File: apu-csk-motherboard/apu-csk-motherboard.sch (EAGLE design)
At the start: 17 parts

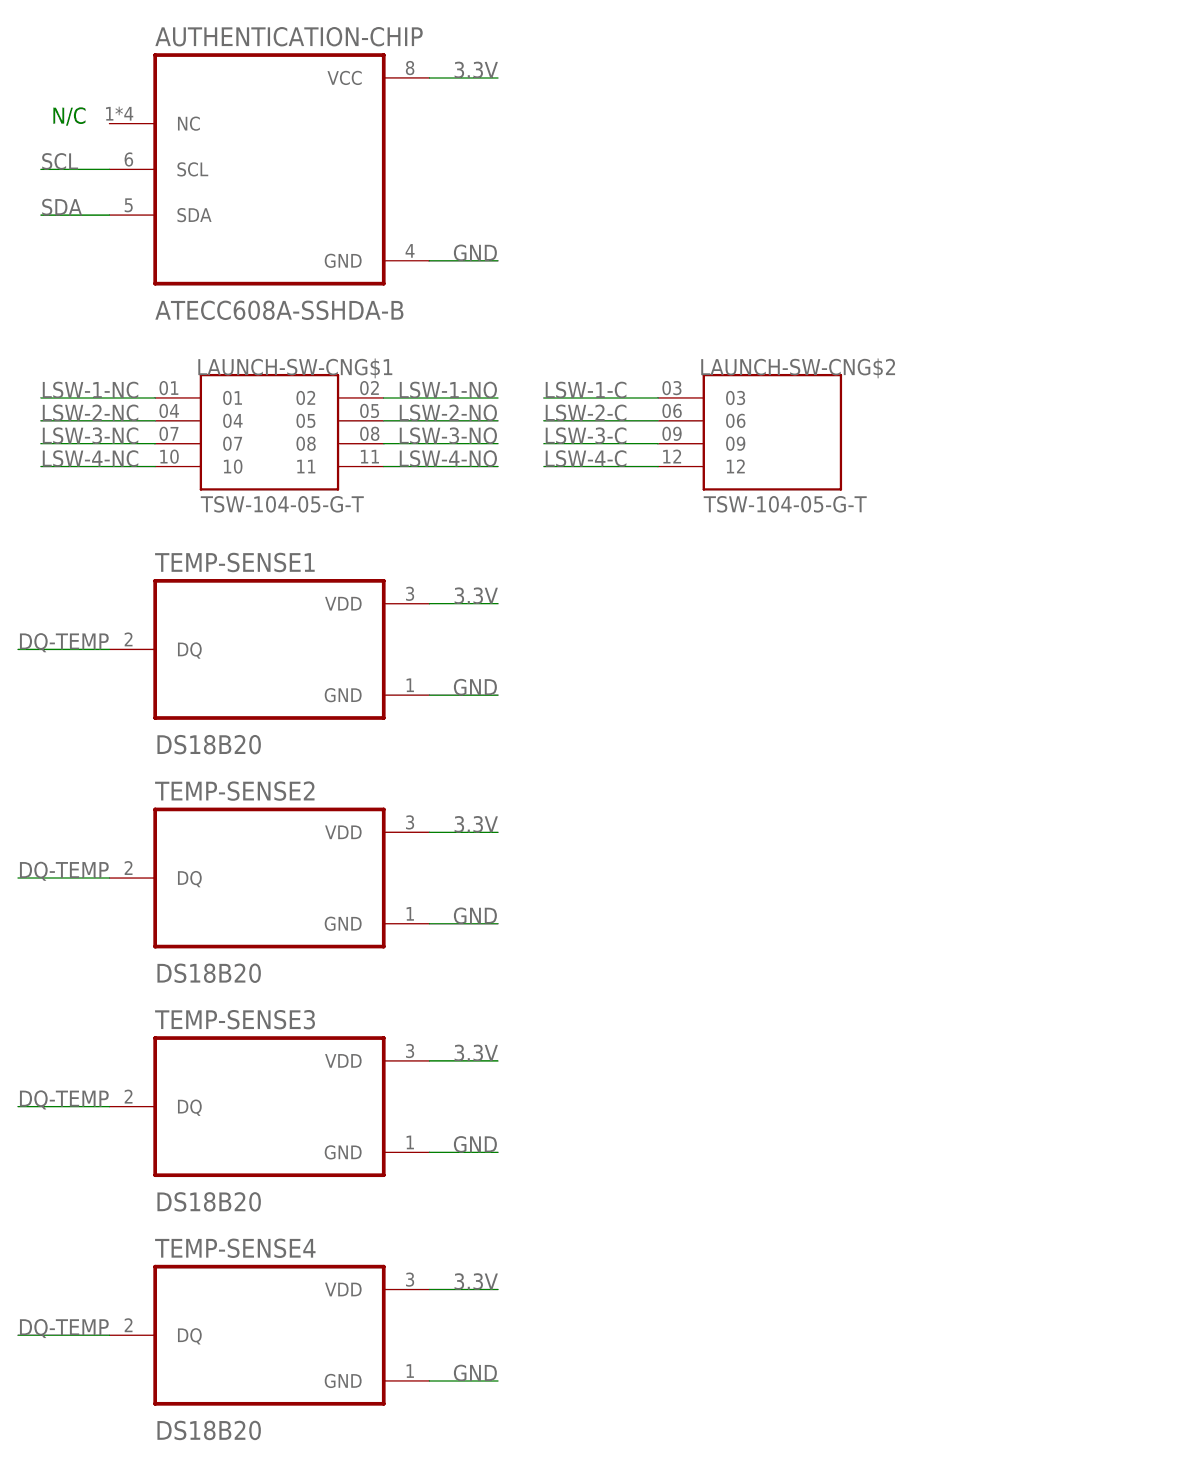
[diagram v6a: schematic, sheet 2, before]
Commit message: Added FRAM and RTC but need to finish connections
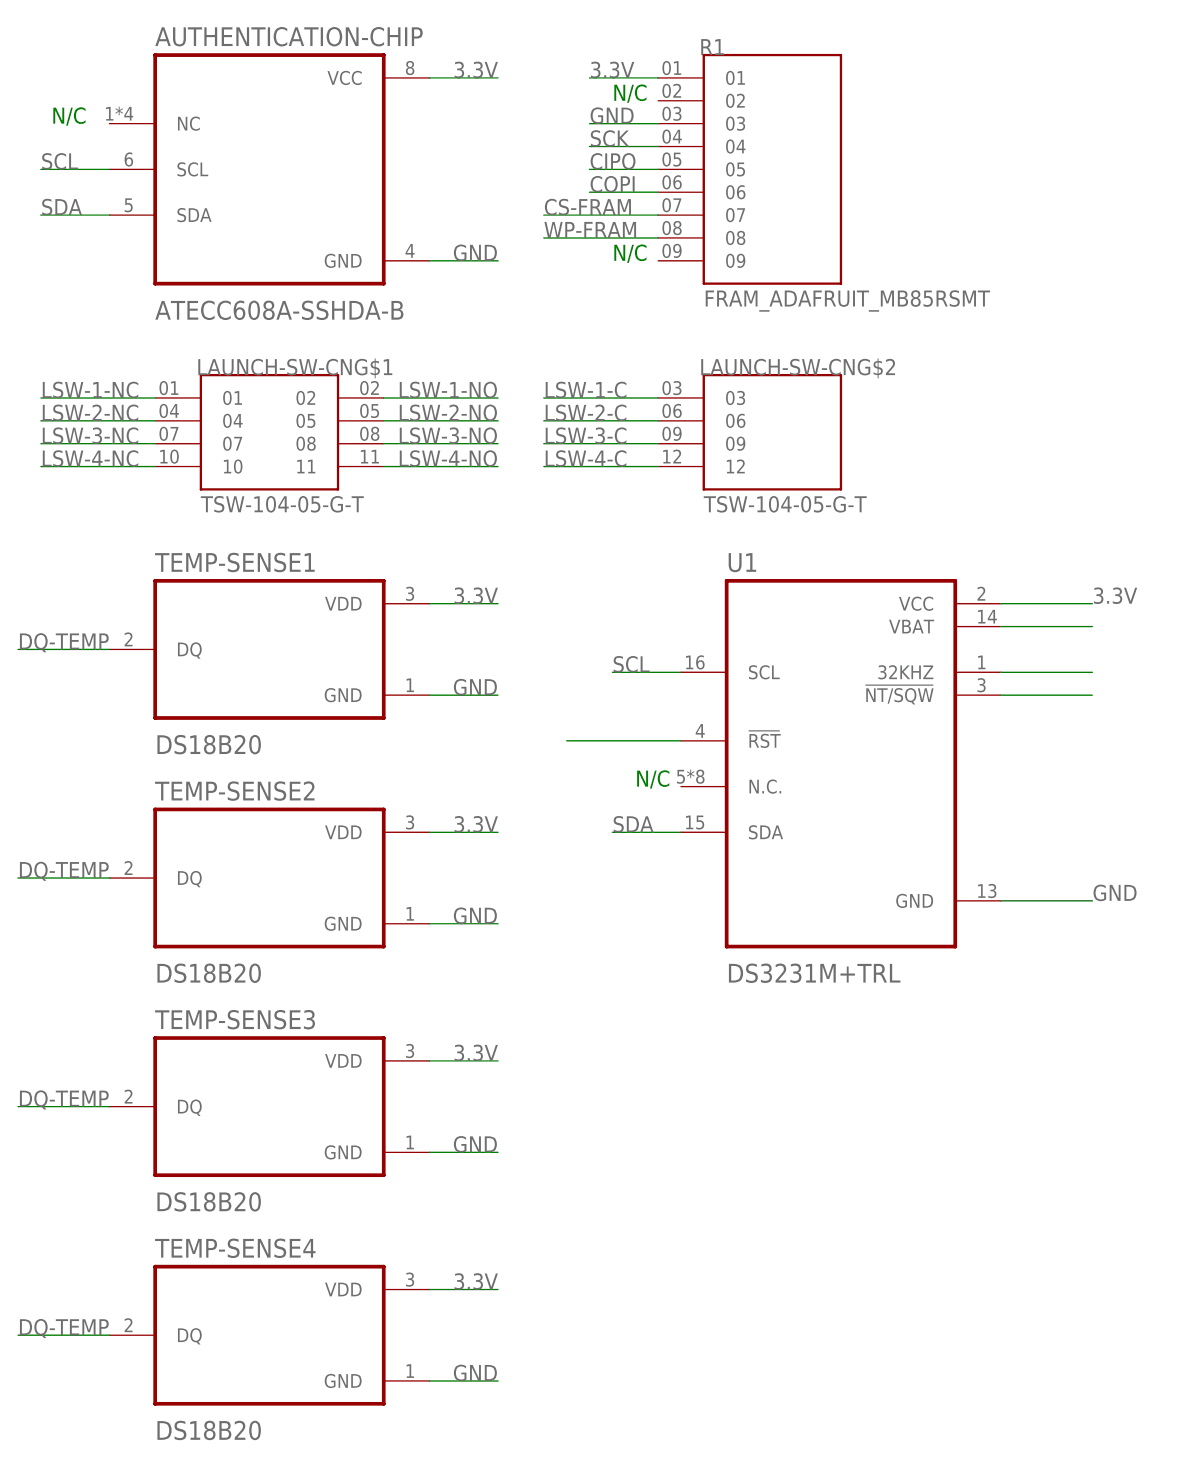
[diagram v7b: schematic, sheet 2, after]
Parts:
- added R1: FRAM_ADAFRUIT_MB85RSMT, apu-csk-motherboard:FRAM_ADAFRUIT_MB85RSMT
- added U1: DS3231M+TRL, DS3231M_TRL:DS3231M+TRL
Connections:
- new net CS-FRAM: FEATHER1-16.IO20@T10, R1.07
- new net N$11: U1.!NT/SQW
- new net N$6: U1.VBAT
- new net N$9: U1.!RST
- new net RTCLOCK: U1.32KHZ
- new net WP-FRAM: FEATHER1-12.IO0@B3, R1.08
- net 3.3V: now also R1.01, U1.VCC
- net CIPO: now also R1.05
- net COPI: now also R1.06
- net GND: now also R1.03, U1.GND
- net SCK: now also R1.04
- net SCL: now also U1.SCL
- net SDA: now also U1.SDA
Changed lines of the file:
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@@
 <layer number="59" name="tCarbon" color="7" fill="1" visible="no" active="no"/>
 <layer number="60" name="bCarbon" color="7" fill="1" visible="no" active="no"/>
+<layer number="61" name="stand" color="7" fill="1" visible="no" active="no"/>
 <layer number="88" name="SimResults" color="9" fill="1" visible="yes" active="yes"/>
 <layer number="89" name="SimProbes" color="9" fill="1" visible="yes" active="yes"/>
@@
 <layer number="112" name="tSilk" color="7" fill="1" visible="no" active="yes"/>
 <layer number="113" name="IDFDebug" color="4" fill="1" visible="no" active="yes"/>
+<layer number="114" name="tPlaceRed" color="7" fill="1" visible="yes" active="yes"/>
+<layer number="115" name="FRNTMAAT2" color="7" fill="1" visible="yes" active="yes"/>
 <layer number="116" name="Patch_BOT" color="9" fill="4" visible="no" active="yes"/>
+<layer number="117" name="BACKMAAT1" color="7" fill="1" visible="yes" active="yes"/>
 <layer number="118" name="Rect_Pads" color="7" fill="1" visible="no" active="yes"/>
+<layer number="119" name="KAP_TEKEN" color="7" fill="1" visible="yes" active="yes"/>
+<layer number="120" name="KAP_MAAT1" color="7" fill="1" visible="yes" active="yes"/>
 <layer number="121" name="_tsilk" color="7" fill="1" visible="no" active="yes"/>
 <layer number="122" name="_bsilk" color="7" fill="1" visible="no" active="yes"/>
@@
 <layer number="128" name="_bValues" color="7" fill="1" visible="no" active="yes"/>
 <layer number="129" name="Mask" color="7" fill="1" visible="no" active="yes"/>
+<layer number="130" name="SMDSTROOK" color="7" fill="1" visible="yes" active="yes"/>
 <layer number="131" name="tAdjust" color="7" fill="1" visible="no" active="yes"/>
 <layer number="132" name="bAdjust" color="7" fill="1" visible="no" active="yes"/>
+<layer number="133" name="bottom_silk" color="7" fill="1" visible="yes" active="yes"/>
+<layer number="134" name="silk_top" color="7" fill="1" visible="no" active="yes"/>
+<layer number="135" name="silk_bottom" color="7" fill="1" visible="no" active="yes"/>
+<layer number="136" name="silktop" color="7" fill="1" visible="no" active="yes"/>
+<layer number="137" name="silkbottom" color="7" fill="1" visible="no" active="yes"/>
+<layer number="138" name="EEE" color="7" fill="1" visible="no" active="yes"/>
+<layer number="139" name="_tKeepout" color="7" fill="1" visible="no" active="yes"/>
+<layer number="140" name="mbKeepout" color="7" fill="1" visible="no" active="yes"/>
+<layer number="141" name="ASSEMBLY_TOP" color="7" fill="1" visible="no" active="yes"/>
+<layer number="142" name="mbRestrict" color="7" fill="1" visible="no" active="yes"/>
+<layer number="143" name="PLACE_BOUND_TOP" color="7" fill="1" visible="no" active="yes"/>
 <layer number="144" name="Drill_legend" color="7" fill="1" visible="no" active="yes"/>
+<layer number="145" name="DrillLegend_01-16" color="7" fill="1" visible="no" active="yes"/>
+<layer number="146" name="DrillLegend_01-20" color="7" fill="1" visible="no" active="yes"/>
+<layer number="147" name="PIN_NUMBER" color="7" fill="1" visible="no" active="yes"/>
+<layer number="148" name="mDocument" color="7" fill="1" visible="no" active="yes"/>
+<layer number="149" name="DrillLegend_02-15" color="7" fill="1" visible="no" active="yes"/>
 <layer number="150" name="Notes" color="7" fill="1" visible="no" active="yes"/>
 <layer number="151" name="HeatSink" color="7" fill="1" visible="no" active="yes"/>
@@
 <layer number="154" name="FabDoc2" color="7" fill="1" visible="no" active="yes"/>
 <layer number="155" name="FabDoc3" color="7" fill="1" visible="no" active="yes"/>
+<layer number="166" name="AntennaArea" color="7" fill="1" visible="no" active="yes"/>
+<layer number="168" name="4mmHeightArea" color="7" fill="1" visible="no" active="yes"/>
+<layer number="191" name="mNets" color="7" fill="1" visible="no" active="yes"/>
+<layer number="192" name="mBusses" color="7" fill="1" visible="no" active="yes"/>
+<layer number="193" name="mPins" color="7" fill="1" visible="no" active="yes"/>
+<layer number="194" name="mSymbols" color="7" fill="1" visible="no" active="yes"/>
+<layer number="195" name="mNames" color="7" fill="1" visible="no" active="yes"/>
+<layer number="196" name="mValues" color="7" fill="1" visible="no" active="yes"/>
 <layer number="199" name="Contour" color="7" fill="1" visible="no" active="yes"/>
 <layer number="200" name="200bmp" color="1" fill="10" visible="no" active="yes"/>
@@
 <part name="TEMP-SENSE4" library="DS18B20" deviceset="DS18B20" device=""/>
 <part name="FRAME3" library="apu-csk-motherboard" deviceset="FRAME_LETTER_LANDSCAPE" device=""/>
+<part name="R1" library="apu-csk-motherboard" deviceset="FRAM_ADAFRUIT_MB85RSMT" device=""/>
+<part name="U1" library="DS3231M_TRL" deviceset="DS3231M+TRL" device=""/>
 </parts>
 <sheets>
@@
 </segment>
 </net>
+<net name="CS-FRAM" class="0">
+<segment>
+<pinref part="FEATHER1" gate="-16" pin="IO20@T10"/>
+<wire x1="154.94" y1="132.08" x2="167.64" y2="132.08" width="0.1524" layer="91"/>
+<label x="154.94" y="132.08" size="1.778" layer="95"/>
+</segment>
+</net>
+<net name="WP-FRAM" class="0">
+<segment>
+<pinref part="FEATHER1" gate="-12" pin="IO0@B3"/>
+<wire x1="154.94" y1="83.82" x2="167.64" y2="83.82" width="0.1524" layer="91"/>
+<label x="154.94" y="83.82" size="1.778" layer="95"/>
+</segment>
+</net>
 </nets>
 </sheet>
@@
 <plain>
 <text x="12.7" y="172.72" size="1.778" layer="91" rot="MR0">N/C</text>
+<text x="71.12" y="175.26" size="1.778" layer="91">N/C</text>
+<text x="71.12" y="157.48" size="1.778" layer="91">N/C</text>
+<text x="73.66" y="99.06" size="1.778" layer="91">N/C</text>
 </plain>
 <instances>
@@
 <attribute name="VALUE" x="20.32" y="26.48" size="2.0828" layer="96" ratio="10" rot="SR0"/>
 </instance>
+<instance part="R1" gate="G$1" x="88.9" y="167.64" smashed="yes">
+<attribute name="NAME" x="80.78" y="180.34" size="1.778" layer="95"/>
+<attribute name="VALUE" x="81.28" y="152.4" size="1.778" layer="96"/>
+</instance>
+<instance part="U1" gate="A" x="96.52" y="101.6" smashed="yes">
+<attribute name="NAME" x="83.82" y="122.92" size="2.0828" layer="95" ratio="10" rot="SR0"/>
+<attribute name="VALUE" x="83.82" y="77.28" size="2.0828" layer="96" ratio="10" rot="SR0"/>
+</instance>
 </instances>
 <busses>
@@
 <label x="58.42" y="157.48" size="1.778" layer="95" rot="MR0"/>
 </segment>
+<segment>
+<wire x1="68.58" y1="172.72" x2="76.2" y2="172.72" width="0.1524" layer="91"/>
+<label x="68.58" y="172.72" size="1.778" layer="95"/>
+<pinref part="R1" gate="G$1" pin="03"/>
+</segment>
+<segment>
+<pinref part="U1" gate="A" pin="GND"/>
+<wire x1="114.3" y1="86.36" x2="124.46" y2="86.36" width="0.1524" layer="91"/>
+<label x="124.46" y="86.36" size="1.778" layer="95"/>
+</segment>
 </net>
 <net name="3.3V" class="0">
@@
 <label x="58.42" y="177.8" size="1.778" layer="95" rot="MR0"/>
 </segment>
+<segment>
+<wire x1="76.2" y1="177.8" x2="68.58" y2="177.8" width="0.1524" layer="91"/>
+<label x="68.58" y="177.8" size="1.778" layer="95"/>
+<pinref part="R1" gate="G$1" pin="01"/>
+</segment>
+<segment>
+<pinref part="U1" gate="A" pin="VCC"/>
+<wire x1="114.3" y1="119.38" x2="124.46" y2="119.38" width="0.1524" layer="91"/>
+<label x="124.46" y="119.38" size="1.778" layer="95"/>
+</segment>
 </net>
 <net name="DQ-TEMP" class="0">
@@
 <label x="7.62" y="162.56" size="1.778" layer="95"/>
 </segment>
+<segment>
+<pinref part="U1" gate="A" pin="SDA"/>
+<wire x1="71.12" y1="93.98" x2="78.74" y2="93.98" width="0.1524" layer="91"/>
+<label x="71.12" y="93.98" size="1.778" layer="95"/>
+</segment>
 </net>
 <net name="SCL" class="0">
@@
 <label x="7.62" y="167.64" size="1.778" layer="95"/>
 </segment>
+<segment>
+<pinref part="U1" gate="A" pin="SCL"/>
+<wire x1="71.12" y1="111.76" x2="78.74" y2="111.76" width="0.1524" layer="91"/>
+<label x="71.12" y="111.76" size="1.778" layer="95"/>
+</segment>
 </net>
 <net name="LSW-1-NO" class="0">
@@
 </segment>
 </net>
+<net name="SCK" class="0">
+<segment>
+<wire x1="68.58" y1="170.18" x2="76.2" y2="170.18" width="0.1524" layer="91"/>
+<label x="68.58" y="170.18" size="1.778" layer="95"/>
+<pinref part="R1" gate="G$1" pin="04"/>
+</segment>
+</net>
+<net name="CIPO" class="0">
+<segment>
+<wire x1="68.58" y1="167.64" x2="76.2" y2="167.64" width="0.1524" layer="91"/>
+<label x="68.58" y="167.64" size="1.778" layer="95"/>
+<pinref part="R1" gate="G$1" pin="05"/>
+</segment>
+</net>
+<net name="COPI" class="0">
+<segment>
+<wire x1="68.58" y1="165.1" x2="76.2" y2="165.1" width="0.1524" layer="91"/>
+<label x="68.58" y="165.1" size="1.778" layer="95"/>
+<pinref part="R1" gate="G$1" pin="06"/>
+</segment>
+</net>
+<net name="CS-FRAM" class="0">
+<segment>
+<wire x1="63.5" y1="162.56" x2="76.2" y2="162.56" width="0.1524" layer="91"/>
+<label x="63.5" y="162.56" size="1.778" layer="95"/>
+<pinref part="R1" gate="G$1" pin="07"/>
+</segment>
+</net>
+<net name="WP-FRAM" class="0">
+<segment>
+<wire x1="63.5" y1="160.02" x2="76.2" y2="160.02" width="0.1524" layer="91"/>
+<label x="63.5" y="160.02" size="1.778" layer="95"/>
+<pinref part="R1" gate="G$1" pin="08"/>
+</segment>
+</net>
+<net name="N$6" class="0">
+<segment>
+<pinref part="U1" gate="A" pin="VBAT"/>
+<wire x1="114.3" y1="116.84" x2="124.46" y2="116.84" width="0.1524" layer="91"/>
+</segment>
+</net>
+<net name="N$9" class="0">
+<segment>
+<pinref part="U1" gate="A" pin="!RST"/>
+<wire x1="66.04" y1="104.14" x2="78.74" y2="104.14" width="0.1524" layer="91"/>
+</segment>
+</net>
+<net name="N$11" class="0">
+<segment>
+<pinref part="U1" gate="A" pin="!NT/SQW"/>
+<wire x1="114.3" y1="109.22" x2="124.46" y2="109.22" width="0.1524" layer="91"/>
+</segment>
+</net>
+<net name="RTCLOCK" class="0">
+<segment>
+<pinref part="U1" gate="A" pin="32KHZ"/>
+<wire x1="114.3" y1="111.76" x2="124.46" y2="111.76" width="0.1524" layer="91"/>
+</segment>
+</net>
